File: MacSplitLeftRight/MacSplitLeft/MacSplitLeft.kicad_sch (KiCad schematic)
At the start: 75 parts, among them J1 AudioJack4, SW1 SW_Push, SW10 SW_Push, SW100 Toggle Mac/Win, SW11 SW_Push, SW12 SW_Push, SW13 SW_Push, SW14 SW_Push, SW15 SW_Push, SW16 SW_Push, SW17 SW_Push, SW18 SW_Push, SW19 SW_Push, SW2 SW_Push, SW20 SW_Push, SW21 SW_Push, SW22 SW_Push, SW23 SW_Push, SW24 SW_Push, SW25 SW_Push, SW26 SW_Push, SW27 SW_Push, SW28 SW_Push, SW29 SW_Push, SW3 SW_Push, SW30 SW_Push, SW4 SW_Push, SW5 SW_Push, SW6 SW_Push, SW7 SW_Push, SW8 SW_Push, SW9 SW_Push, U2 KB2040

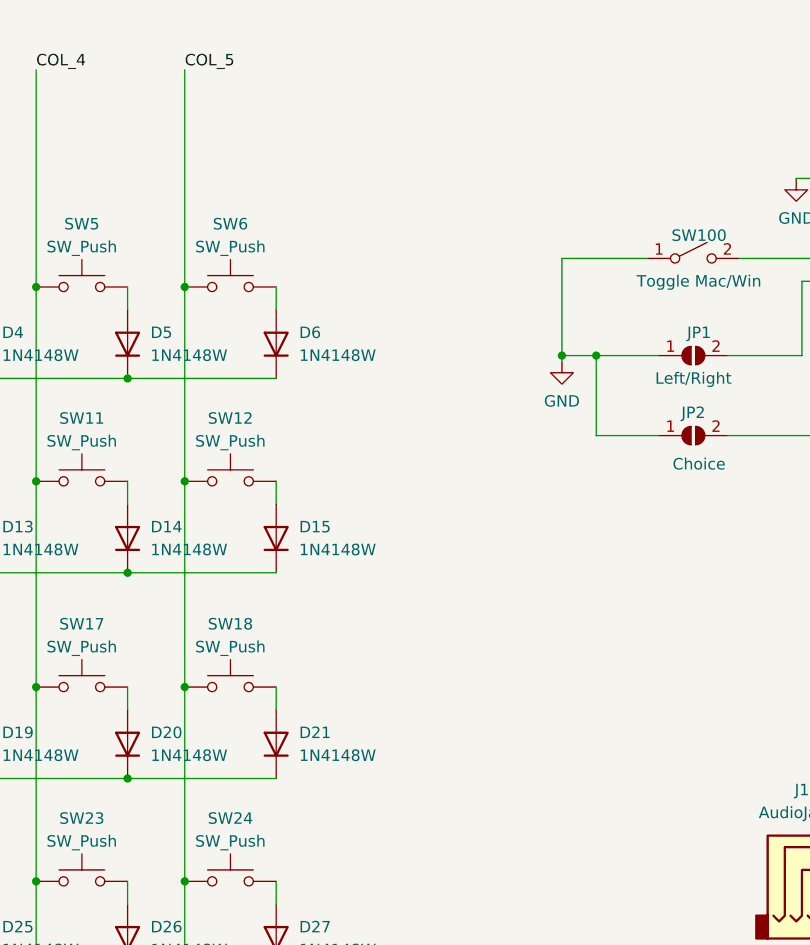
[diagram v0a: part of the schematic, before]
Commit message: Left 32 keys
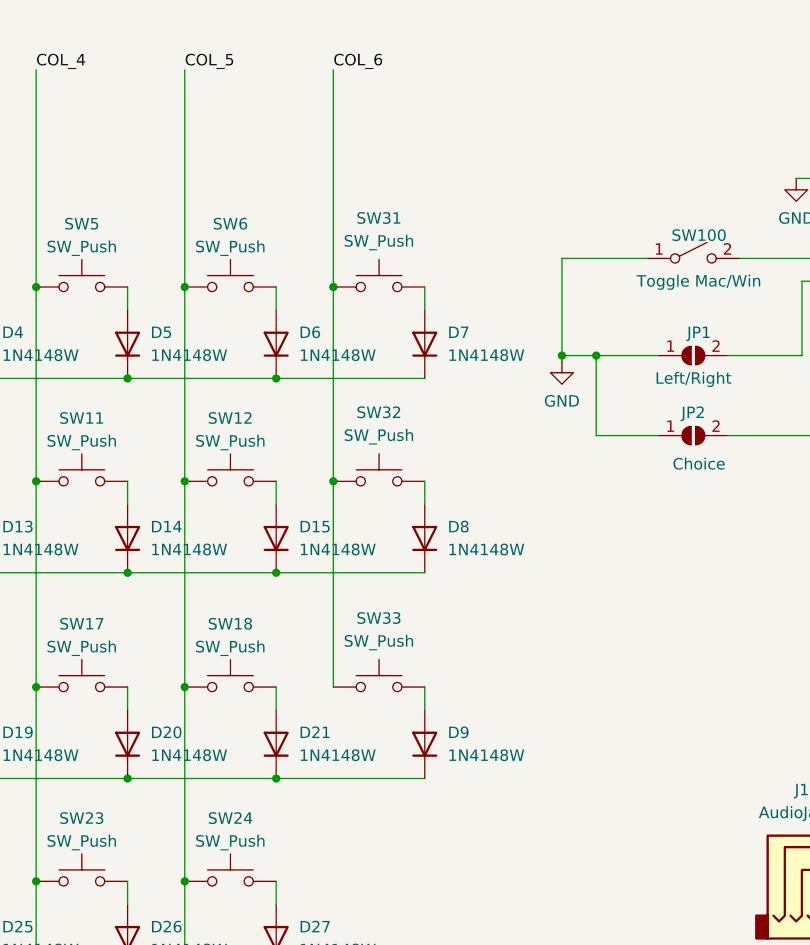
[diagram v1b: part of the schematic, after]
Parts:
- added D7, D8, D9: 1N4148W, Diode_SMD:D_SOD-323_Hand_Split_Keyboard, symbol Diode:1N4148W
- added SW31, SW32, SW33: SW_Push, Lily58-footprint:MX_PG1350-DoubleSide_Keycap_28mm_1.50u, symbol Switch:SW_Push
- SW13, SW19, SW27, SW28, SW29, SW30: footprint Lily58-footprint:MX_PG1350-DoubleSide_Keycap_28mm_1.50u -> Lily58-footprint:MX_PG1350-DoubleSide_Keycap_18mm_1.00u
- SW25: footprint Lily58-footprint:MX_PG1350-DoubleSide_Keycap_18mm_1.00u -> Lily58-footprint:MX_PG1350-DoubleSide_Keycap_28mm_1.50u
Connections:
- net ROW_0: now also D7.1 (K)
- net ROW_1: now also D8.1 (K)
- net ROW_2: now also D9.1 (K)
- new net: D8.2 (A), SW32.2
- new net: D9.2 (A), SW33.2
- new net: D7.2 (A), SW31.2
- new net COL_6: SW31.1, SW32.1, SW33.1

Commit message: Position readjustments
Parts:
- SW29: footprint Lily58-footprint:MX_PG1350-DoubleSide_Keycap_18mm_1.00u -> Lily58-footprint:MX_PG1350-DoubleSide_Keycap_28mm_1.50u
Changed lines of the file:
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@@
     (property "Reference" "SW29" (id 0) (at 113.665 135.255 0))
     (property "Value" "SW_Push" (id 1) (at 113.665 137.795 0))
-    (property "Footprint" "Lily58-footprint:MX_PG1350-DoubleSide_Keycap_18mm_1.00u" (id 2) (at 113.665 137.16 0)
+    (property "Footprint" "Lily58-footprint:MX_PG1350-DoubleSide_Keycap_28mm_1.50u" (id 2) (at 113.665 137.16 0)
       (effects (font (size 1.27 1.27)) hide)
     )
@@
     )
     (path "/b209455e-4689-40c6-9c5f-6ad42f23df4f"
-      (reference "SW29") (unit 1) (value "SW_Push") (footprint "Lily58-footprint:MX_PG1350-DoubleSide_Keycap_18mm_1.00u")
+      (reference "SW29") (unit 1) (value "SW_Push") (footprint "Lily58-footprint:MX_PG1350-DoubleSide_Keycap_28mm_1.50u")
     )
     (path "/cf30b61b-518f-4fc0-9759-5e2e77a579bf"
